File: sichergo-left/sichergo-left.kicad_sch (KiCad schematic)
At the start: 39 parts, among them J1 Conn_01x04_Pin, Q1 2N7002, SW19 MS-22C01-G010, U1 AZ1117-3.3, U2 TPD4E05U06DQA, U3 YTS1C0033BBG01, U4 STM32F103C8Tx, U5 SN74LVC1G125DBV, U6 SN74LVC1G125DBV, Y1 Crystal_GND24

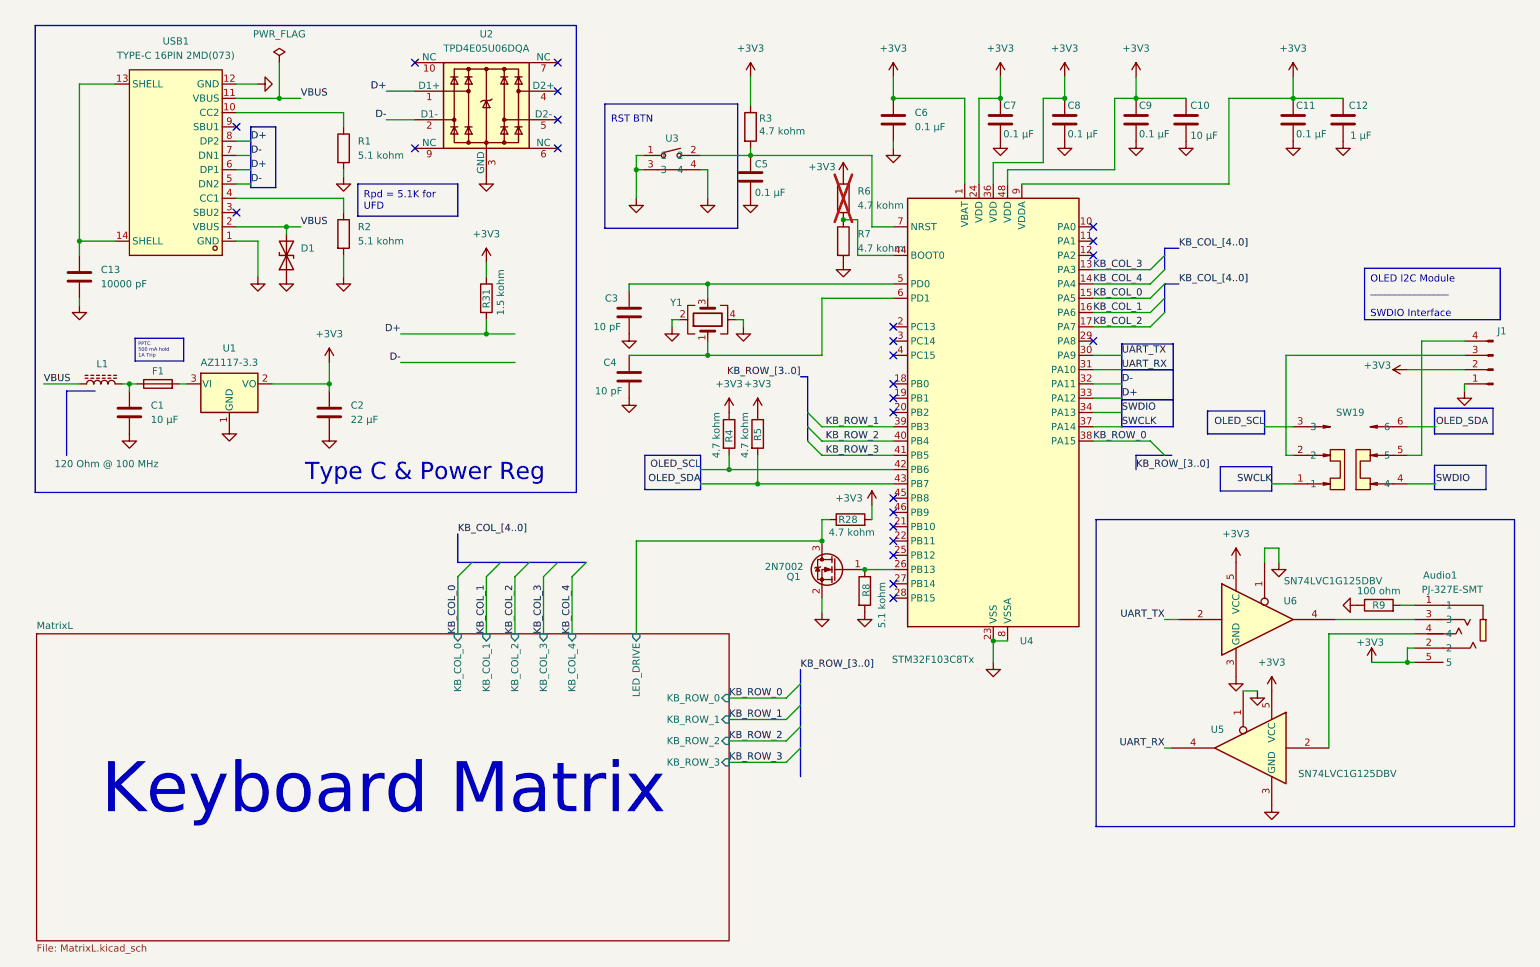
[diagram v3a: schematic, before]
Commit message: Finish routing LEFT side
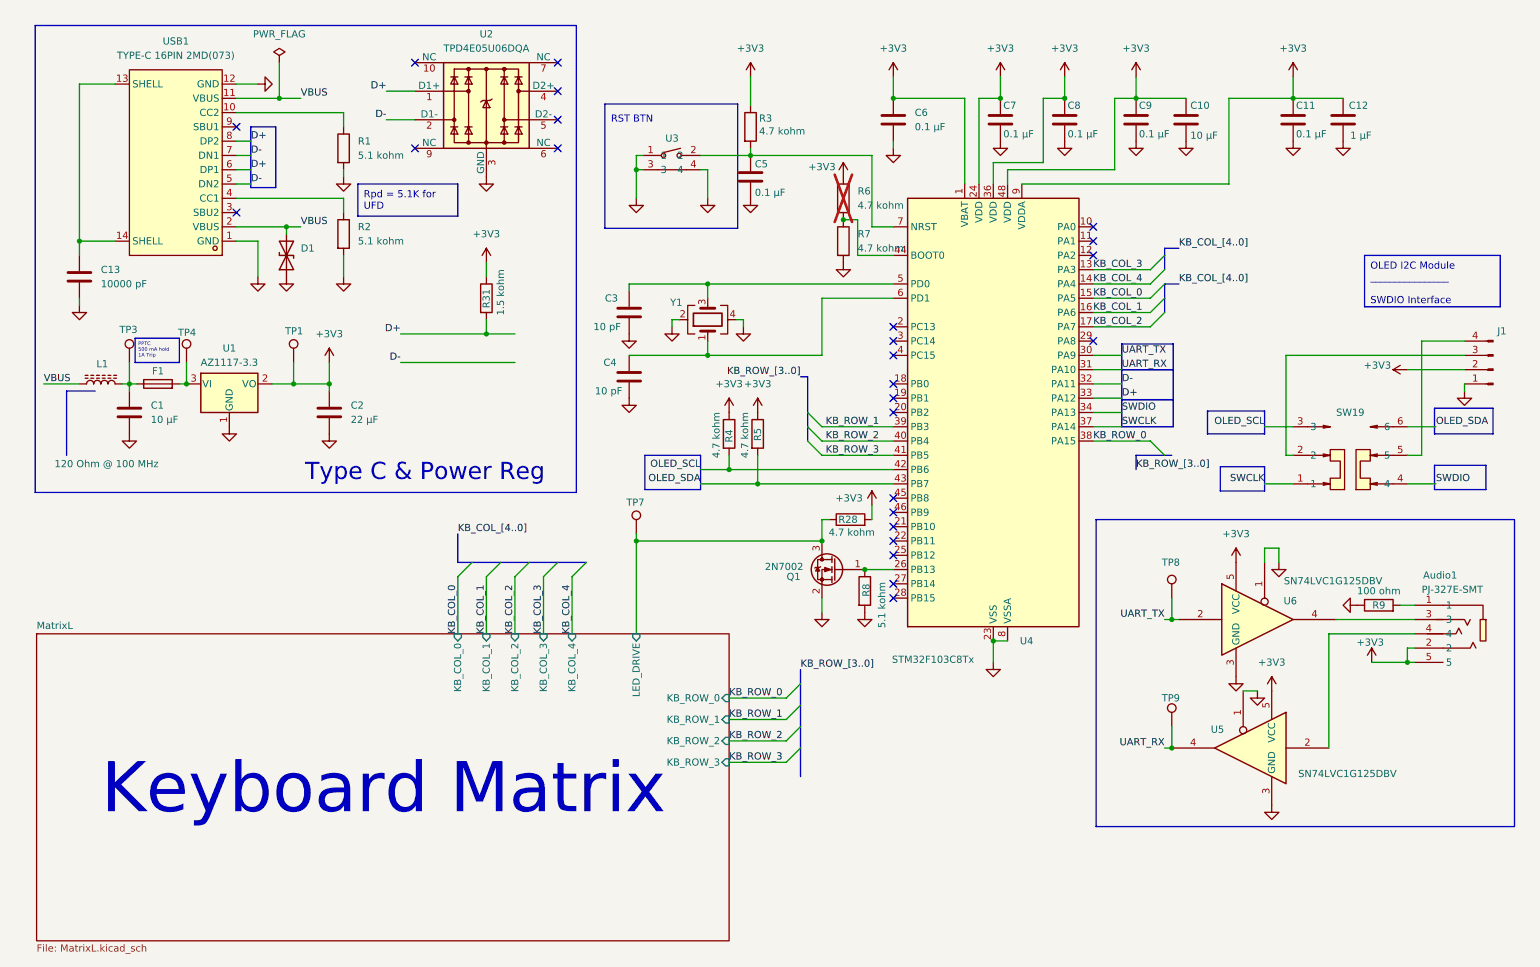
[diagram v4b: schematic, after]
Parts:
- added TP1, TP3, TP4, TP7, TP8, TP9: TestPoint, TestPoint:TestPoint_THTPad_1.0x1.0mm_Drill0.5mm, symbol Connector:TestPoint
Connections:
- net +3V3: now also TP1.1
- net MatrixL/LED_DRIVE: now also TP7.1
- net UART_RX: now also TP9.1
- net UART_TX: now also TP8.1
- net at C1.1, F1.1, L1.2: now also TP3.1
- net at F1.2, U1.3 (VI): now also TP4.1

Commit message: Remake entire shape
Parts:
- Audio1: InvenTree (none) -> 75
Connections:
- net +3V3: now also R28.1; no longer R28.2
- net KB_ROW_0: now also U4.21 (PB10); no longer U4.38 (PA15)
- net KB_ROW_1: now also U4.18 (PB0); no longer U4.39 (PB3)
- net KB_ROW_2: now also U4.19 (PB1); no longer U4.40 (PB4)
- net KB_ROW_3: now also U4.20 (PB2); no longer U4.41 (PB5)
- net MatrixL/LED_DRIVE: now also R28.2; no longer R28.1
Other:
- moved on the sheet: R28

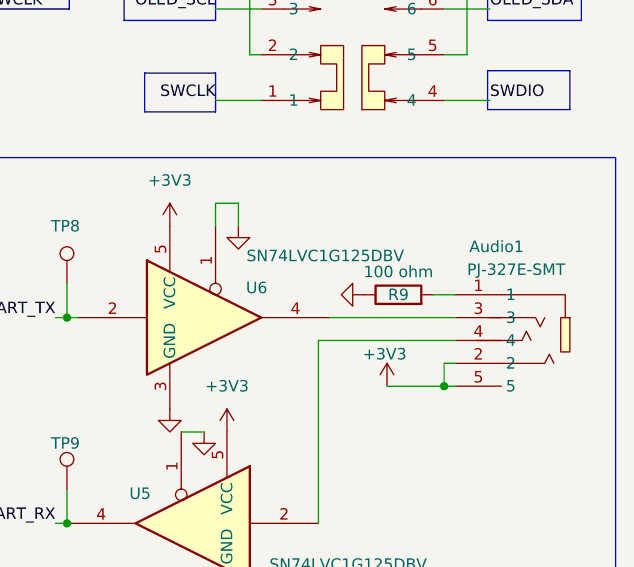
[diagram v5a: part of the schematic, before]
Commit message: Fix keyboard layout size
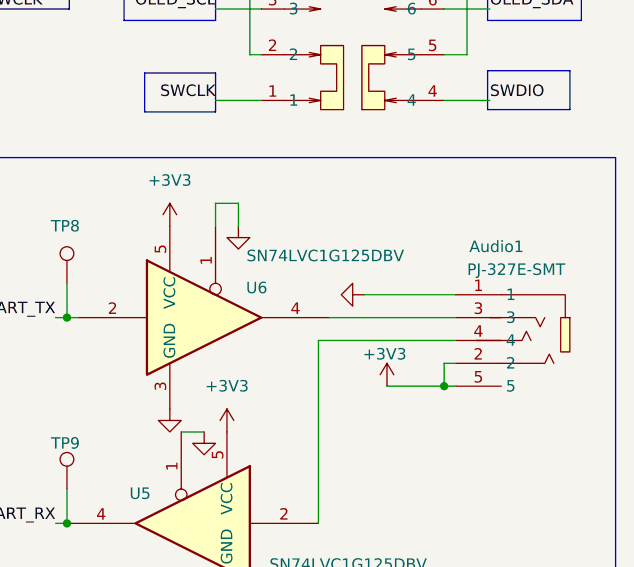
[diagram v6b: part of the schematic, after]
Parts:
- removed R9: 100 ohm, Resistor_SMD:R_0603_1608Metric_Pad0.98x0.95mm_HandSolder, symbol #inventree:RC0603FR-07100RL
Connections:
- net GND: now also Audio1.1
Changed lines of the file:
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@@
 	(wire
 		(pts
-			(xy 260.35 123.19) (xy 262.89 123.19)
-		)
-		(stroke
-			(width 0)
-			(type default)
-		)
-	)
-	(wire
-		(pts
 			(xy 34.29 80.01) (xy 34.29 83.82)
 		)
@@
 	(wire
 		(pts
+			(xy 252.73 123.19) (xy 262.89 123.19)
+		)
+		(stroke
+			(width 0)
+			(type default)
+		)
+	)
+	(wire
+		(pts
 			(xy 25.4 30.48) (xy 25.4 58.42)
 		)
@@
 					(unit 1)
 				)
-			)
-		)
-	)
-	(symbol
-		(lib_id "#inventree:RC0603FR-07100RL")
-		(at 256.54 123.19 90)
-		(unit 1)
-		(exclude_from_sim no)
-		(in_bom yes)
-		(on_board yes)
-		(dnp no)
-		(property "Reference" "R9"
-			(at 256.54 123.19 90)
-			(effects
-				(font
-					(size 1.27 1.27)
-				)
-			)
-		)
-		(property "Value" "100 ohm"
-			(at 256.54 120.65 90)
-			(effects
-				(font
-					(size 1.27 1.27)
-				)
-			)
-		)
-		(property "Footprint" "Resistor_SMD:R_0603_1608Metric_Pad0.98x0.95mm_HandSolder"
-			(at 256.54 124.968 90)
-			(effects
-				(font
-					(size 1.27 1.27)
-				)
-				(hide yes)
-			)
-		)
-		(property "Datasheet" "http://10.0.0.41/media/attachments/part/71/PYu-RC_Group_51_RoHS_L_12.pdf"
-			(at 256.54 123.19 0)
-			(effects
-				(font
-					(size 1.27 1.27)
-				)
-				(hide yes)
-			)
-		)
-		(property "Description" "RES 100 OHM 1% 1/10W 0603"
-			(at 256.54 123.19 0)
-			(effects
-				(font
-					(size 1.27 1.27)
-				)
-				(hide yes)
-			)
-		)
-		(property "InvenTree" "71"
-			(at 256.54 123.19 0)
-			(effects
-				(font
-					(size 1.27 1.27)
-				)
-				(hide yes)
-			)
-		)
-		(property "Mounting Type" "0603"
-			(at 256.54 123.19 0)
-			(effects
-				(font
-					(size 1.27 1.27)
-				)
-				(hide yes)
-			)
-		)
-		(property "Package Type" "0603 (1608 Metric)"
-			(at 256.54 123.19 0)
-			(effects
-				(font
-					(size 1.27 1.27)
-				)
-				(hide yes)
-			)
-		)
-		(property "Part URL" "http://10.0.0.41:7333/part/71/"
-			(at 256.54 123.19 0)
-			(effects
-				(font
-					(size 1.27 1.27)
-				)
-				(hide yes)
-			)
-		)
-		(property "Rated Power" "0.1W, 1/10W"
-			(at 256.54 123.19 0)
-			(effects
-				(font
-					(size 1.27 1.27)
-				)
-				(hide yes)
-			)
-		)
-		(property "Tolerance" "1%"
-			(at 256.54 123.19 0)
-			(effects
-				(font
-					(size 1.27 1.27)
-				)
-				(hide yes)
-			)
-		)
-		(pin "2"
-		)
-		(pin "1"
-		)
-		(instances
-			(project ""
-				(path "/7d6715fb-1e77-4b7f-bc05-ec156d7f2ccd"
-					(reference "R9")
-					(unit 1)
-				)

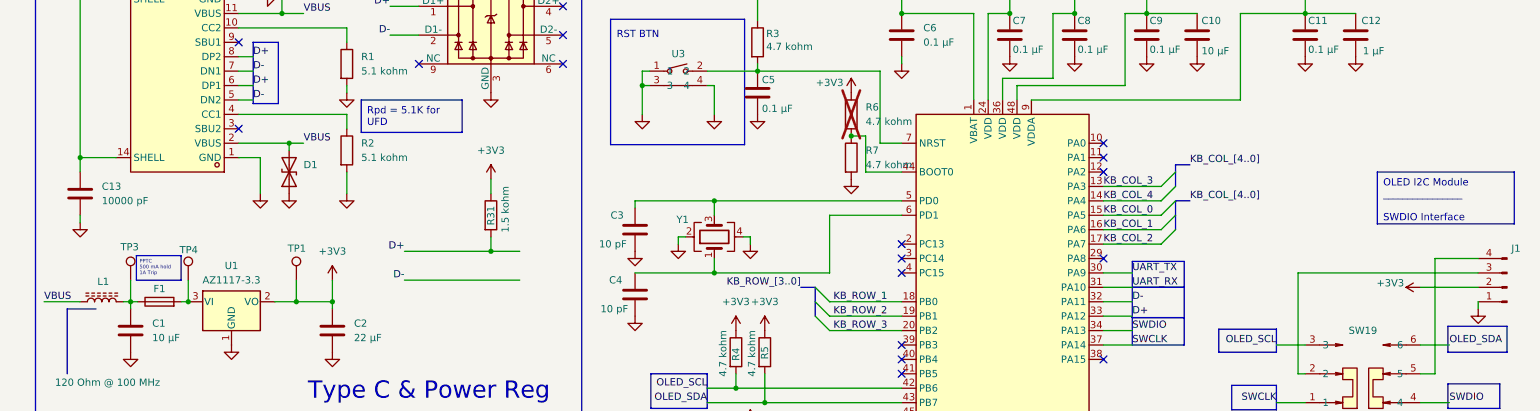
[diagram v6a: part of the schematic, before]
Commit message: fix left side USB C
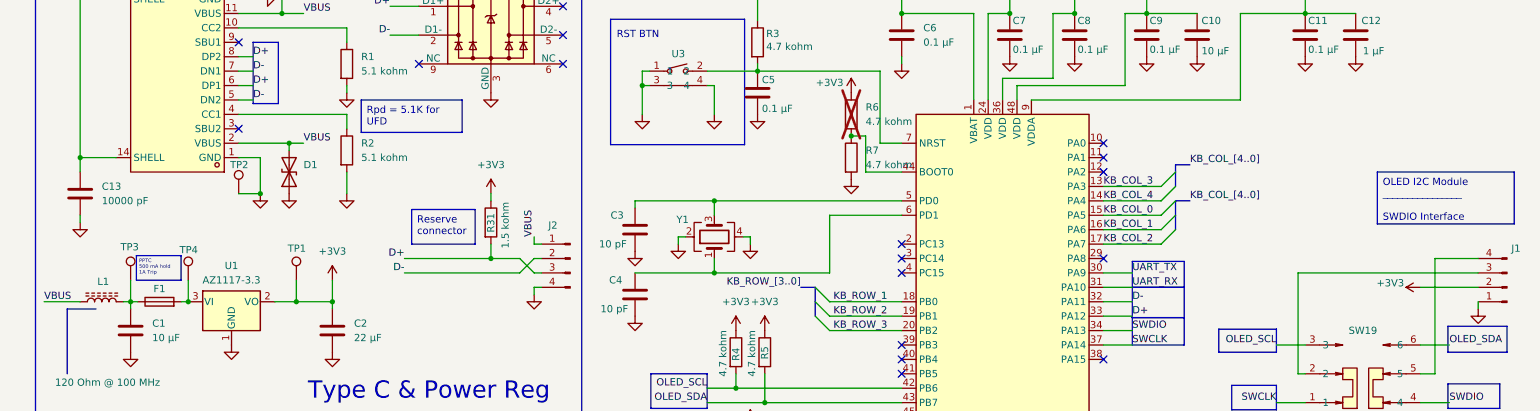
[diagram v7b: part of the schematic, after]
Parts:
- added J2: Conn_01x04_Pin, Connector_PinSocket_2.54mm:PinSocket_1x04_P2.54mm_Vertical, symbol Connector:Conn_01x04_Pin
- added TP2: TestPoint, TestPoint:TestPoint_THTPad_1.0x1.0mm_Drill0.5mm, symbol Connector:TestPoint
- L1: InvenTree (none) -> 74
- SW19: InvenTree (none) -> 62
- U2: InvenTree (none) -> 56
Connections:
- net D+: now also J2.3 (Pin_3)
- net D-: now also J2.2 (Pin_2)
- net GND: now also J2.4 (Pin_4), TP2.1
- net VBUS: now also J2.1 (Pin_1)
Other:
- moved on the sheet: R31
